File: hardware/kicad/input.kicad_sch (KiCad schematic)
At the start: 16 parts, among them J1 NRJ6HF, J2 NRJ6HF, U1 THAT1246S08, U2 THAT1246S08

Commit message: Add routed PCB layout, gerbers and PCB section on the site
- ghost-fader.kicad_pcb: 2-layer 108 x 80 mm board for the Hammond 1590BB,
  corner notches for the lid-screw bosses, jacks on the rear edge, Teensy USB
  flush with the front edge, DC-DC front-centre. Ground pour both layers,
  0.6 mm power / 0.3 mm signal tracks. DRC clean with schematic parity.
- tools/build_pcb.py (placement table, outline, pours, rules) and
  tools/route.py (Freerouting DSN/SES round trip) to regenerate the board.
- Jacks assigned KiCad's stock Neutrik NRJ6HF footprint; BOM regenerated.
- Design rules and Power net class in the project file and gen.py.
- Gerbers, drill and drill map in hardware/gerbers plus a zip for upload.
- Renders in docs/pcb and a PCB layout section on the published page;
  README PCB section.

Co-Authored-By: Claude Fable 5.1 <noreply@anthropic.com>
Claude-Session: https://claude.ai/code/session_015P372fhz9Ee8MTRWGXMeho
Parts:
- J1, J2: footprint (none) -> Connector_Audio:Jack_6.35mm_Neutrik_NRJ6HF_Horizontal
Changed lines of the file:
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@@
   (property "Reference" "J1" (at 34.29 45.72 0) (effects (font (size 1.27 1.27)) (justify left)))
   (property "Value" "NRJ6HF" (at 34.29 62.23 0) (effects (font (size 1.27 1.27)) (justify left)))
-  (property "Footprint" "" (at 40.64 50.8 0) (effects (font (size 1.27 1.27)) (hide yes)))
+  (property "Footprint" "Connector_Audio:Jack_6.35mm_Neutrik_NRJ6HF_Horizontal" (at 40.64 50.8 0) (effects (font (size 1.27 1.27)) (hide yes)))
   (property "Datasheet" "" (at 40.64 50.8 0) (effects (font (size 1.27 1.27)) (hide yes)))
   (pin "R")
@@
   (property "Reference" "J2" (at 34.29 111.76 0) (effects (font (size 1.27 1.27)) (justify left)))
   (property "Value" "NRJ6HF" (at 34.29 128.27 0) (effects (font (size 1.27 1.27)) (justify left)))
-  (property "Footprint" "" (at 40.64 116.84 0) (effects (font (size 1.27 1.27)) (hide yes)))
+  (property "Footprint" "Connector_Audio:Jack_6.35mm_Neutrik_NRJ6HF_Horizontal" (at 40.64 116.84 0) (effects (font (size 1.27 1.27)) (hide yes)))
   (property "Datasheet" "" (at 40.64 116.84 0) (effects (font (size 1.27 1.27)) (hide yes)))
   (pin "R")

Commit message: Rev C: XIAO RP2040 and Traco TBA 2-0522 replace the Teensy 4.0 and TMR 3
Tier 1 cost-down, no change to the audio path. U9 becomes a Seeed XIAO
RP2040 on header pins (USB-C, TinyUSB MIDI, its 5V pin is VBUS straight
through), PS1 becomes a 2 W unregulated Traco TBA 2-0522 on KiCad's stock
SIP-7 footprint. Rails are now +/-12 V: the +/-15 V TBA 2-0523 would pass
the PGA2310's 16 V absolute maximum at light load. Parts cost drops from
about $145 to about $110.

- gen.py: TBA2_Dual and XIAO_RP2040 symbols, XIAO footprint (Seeed pin
  numbering, USB-C overhang drawn), control sheet rewired to D0-D10,
  power sheet and notes for the unregulated converter, +/-12V rails.
- check.py: new U9 / PS1 pins; NETLIST OK. ERC 0/0.
- Both boards rebuilt and re-routed (Freerouting 1.9), DRC 0 errors; the
  only warnings are jack-nose and USB-C shell silk over the board edge.
- Gerbers, drill, zips, BOM, schematic SVG/PDF and board renders
  regenerated. README and site updated: pin map, power budget
  (~250 mA typical), level budget at +/-12 V, parts list and totals.

Co-Authored-By: Claude Fable 5.1 <noreply@anthropic.com>
Claude-Session: https://claude.ai/code/session_01C8uqpe49go1TPWMsWKKVkn
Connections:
- net +15V renamed +12V
- net -15V renamed -12V

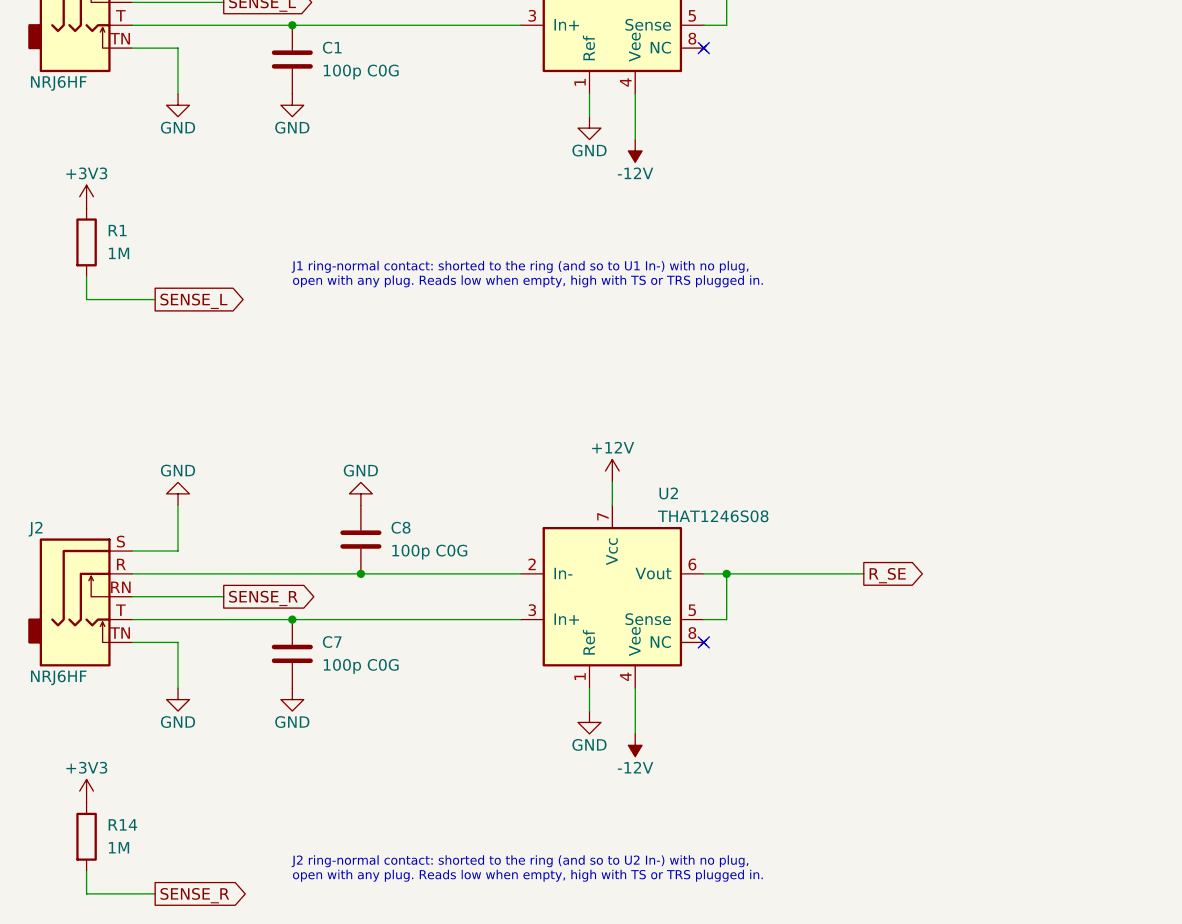
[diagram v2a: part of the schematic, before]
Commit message: Rev D: isolate the audio ground from USB
Add a TI ISO7762FDW digital isolator on the four control lines and two
plug-sense lines, a 78L05 that makes +5VA from +12 V for the PGA logic
and the isolator's audio side, and a split ground: GND_USB (XIAO, USB-C,
switch, LED, ferrite, reservoir, DC-DC input) and GND (everything audio).
The two meet only through C45 (1 nF) and R17 (1 M) at PS1. The sense
pull-ups drop from 1 M to 100 k for the isolator's input leakage.

Both boards get two ground pours per layer with a 2 mm copper-free gap
and a rule area that keeps the router out; U8 and PS1 straddle the gap.
The 1590BB board's island is the front-left corner; the narrow board's
is a pocket under the XIAO with the audio ground wrapping beneath it.
ERC 0, netlist checked (61 nets, 263 pins), DRC clean on both routed
boards, and a script check confirms no copper crosses the gap.

README, docs page, schematic exports, renders, gerbers and BOM regenerated.

Co-Authored-By: Claude Fable 5.1 <noreply@anthropic.com>
Claude-Session: https://claude.ai/code/session_013C8baRPktSQjwfdzSRwmAq
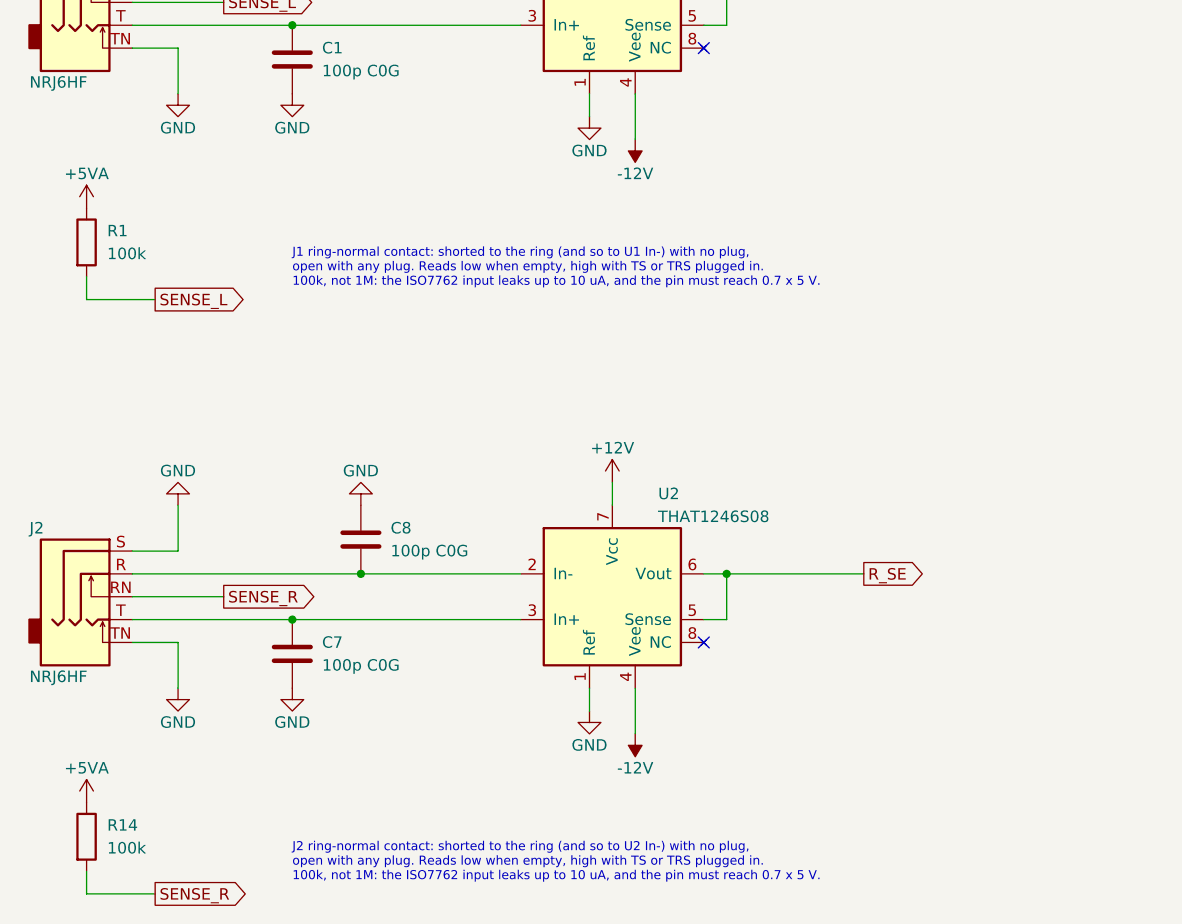
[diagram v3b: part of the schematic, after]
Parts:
- R1, R14: value 1M -> 100k
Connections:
- net +3V3 renamed +5VA
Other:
- note added: "J1 ring-normal contact: shorted to the ring (and so to U1 In-) with no plug, open with any plug. Reads low when empty, high with TS or TRS plugged in. 100k, not 1M: the ISO7762 input leaks up to 10 uA, and the pin must reach 0.7 x 5 V."
- note added: "J2 ring-normal contact: shorted to the ring (and so to U2 In-) with no plug, open with any plug. Reads low when empty, high with TS or TRS plugged in. 100k, not 1M: the ISO7762 input leaks up to 10 uA, and the pin must reach 0.7 x 5 V."
- note removed: "J1 ring-normal contact: shorted to the ring (and so to U1 In-) with no plug, open with any plug. Reads low when empty, high with TS or TRS plugged in."
- note removed: "J2 ring-normal contact: shorted to the ring (and so to U2 In-) with no plug, open with any plug. Reads low when empty, high with TS or TRS plugged in."
